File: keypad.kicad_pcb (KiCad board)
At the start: 2 copper layers, 3.6 x 3.2 mm, 14 parts, among them J1 Capacitive touch buttons, SW1 SW_Push, SW2 SW_Push, SW3 SW_Push, U1 XIAO-ESP32-S3

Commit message: fixed pcb wiring sorry!!
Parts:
- removed the J1 at (69.0, 128.0)
- removed the J1 at (159.0, 109.0)
- removed the J1 at (124.0, 110.0)
- removed the J1 at (140.0, 128.0)
- removed the J1 at (176.0, 128.0)
- added ?: , , F.Cu at (110.0, 86.0)
- added ?: , , F.Cu at (124.0, 132.0)
- added ?: , , F.Cu at (141.0, 89.0)
- added ?: , , F.Cu at (157.0, 129.0)
- added ?: , , F.Cu at (61.0, 132.0)
- moved D3 58.4 mm to (64.0, 50.0)
- moved U1 55.9 mm to (90.0, 59.0), turned to 90 degrees
- moved D2 37.3 mm to (64.0, 58.0)
- moved SW1 36.0 mm to (114.0, 59.1)
- moved SW2 36.0 mm to (135.0, 59.1)
- moved SW3 36.0 mm to (156.0, 59.1)
- moved ? 18.7 mm to (93.0, 128.6)
- moved D1 18.5 mm to (64.0, 66.0)
- moved J1 12.9 mm to (76.0, 103.3)
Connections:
- U1 pad 10: /SWITCH3 -> /LED
- U1 pad 11: /LED -> /TOUCH7
- U1 pad 9: /TOUCH7 -> /SWITCH3
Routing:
- net /TOUCH7: track 0.00 -> 125.6 mm
- net GND: track 0.00 -> 121.3 mm, vias 0 -> 1
- net /TOUCH5: track 0.00 -> 90.6 mm
- net /TOUCH1: track 0.00 -> 85.2 mm
- net /TOUCH3: track 0.00 -> 64.3 mm
- net /SWITCH3: track 0.00 -> 60.6 mm
- net /TOUCH6: track 0.00 -> 55.1 mm
- net +3.3V: track 0.00 -> 43.8 mm, vias 0 -> 3
- net /LED: track 0.00 -> 38.3 mm
- net /SWITCH2: track 0.00 -> 37.1 mm
- net Net-(D1-DOUT): track 0.00 -> 32.1 mm, vias 0 -> 2
- net /TOUCH4: track 0.00 -> 27.9 mm
- net /TOUCH2: track 0.00 -> 25.1 mm
- net Net-(D2-DOUT): track 0.00 -> 23.2 mm, vias 0 -> 2
- net /SWITCH1: track 0.00 -> 12.9 mm

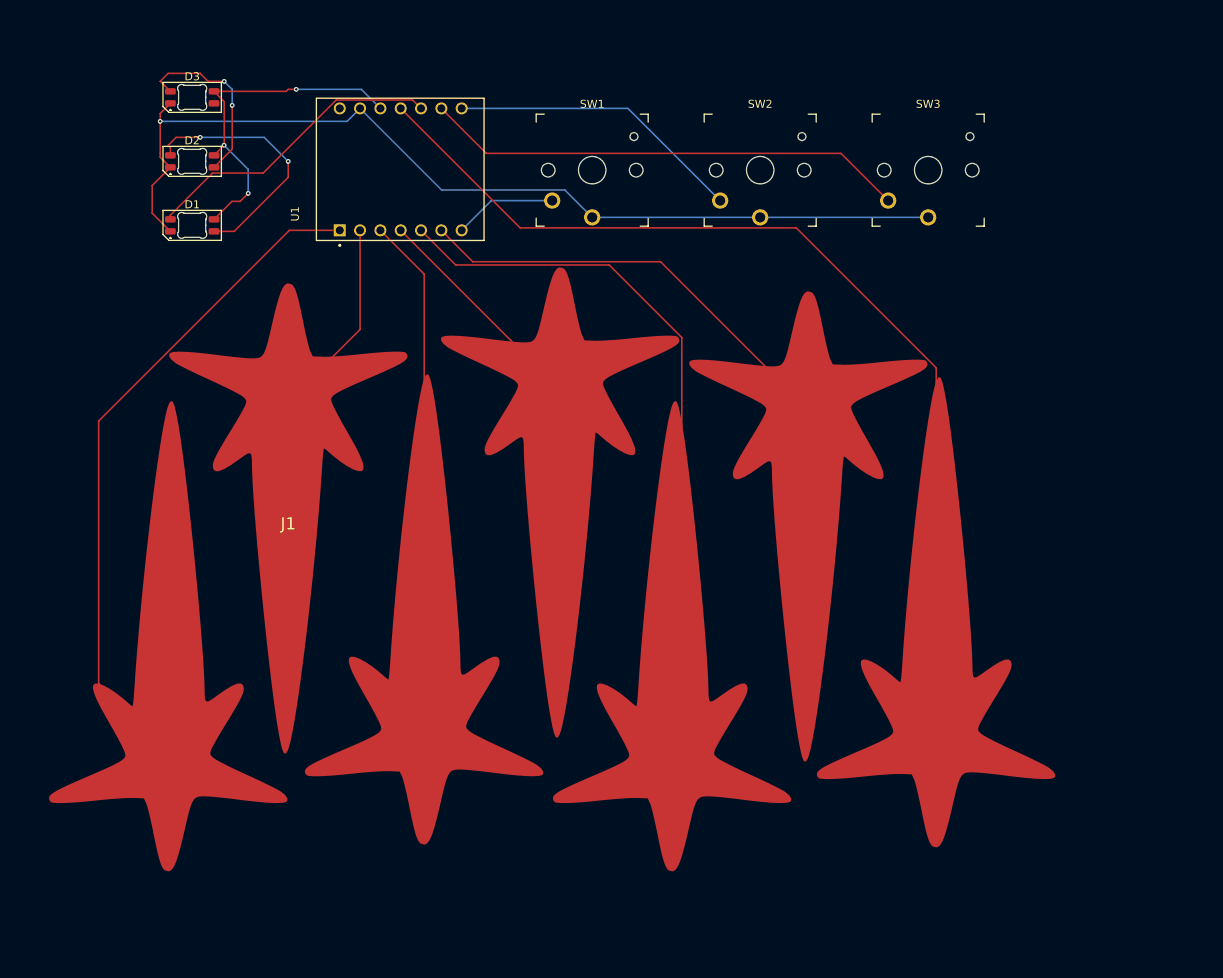
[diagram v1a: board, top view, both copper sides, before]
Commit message: fixed silkscreen
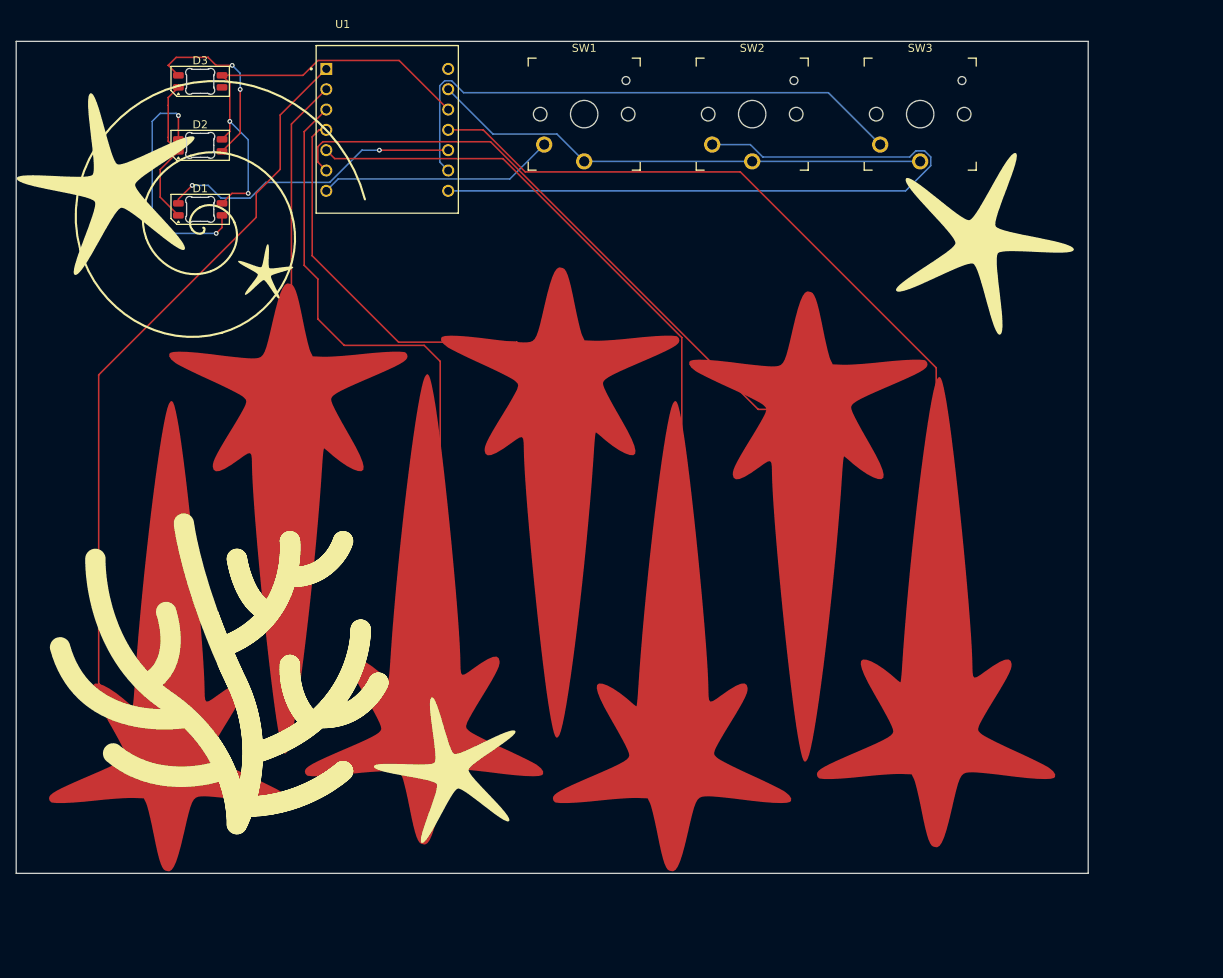
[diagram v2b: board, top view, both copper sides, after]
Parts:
- moved SW1 7.07 mm to (113.0, 52.1)
- moved SW2 7.07 mm to (134.0, 52.1)
- moved SW3 7.07 mm to (155.0, 52.1)
- moved U1 5.26 mm to (88.4, 54.0), turned to 0 degrees
- moved D1 2.24 mm to (65.0, 64.0)
- moved D2 2.24 mm to (65.0, 56.0)
- moved D3 2.24 mm to (65.0, 48.0)
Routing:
- net /SWITCH2: track 37.1 -> 91.3 mm
- net GND: track 121.3 -> 81.7 mm, vias 1 -> 0
- net /TOUCH3: track 64.3 -> 92.0 mm
- net /TOUCH4: track 27.9 -> 54.7 mm
- net /TOUCH6: track 55.1 -> 78.8 mm
- net /SWITCH1: track 12.9 -> 29.6 mm
- net /TOUCH5: track 90.6 -> 106.6 mm
- net /TOUCH2: track 25.1 -> 41.0 mm
- net /TOUCH1: track 85.2 -> 100.9 mm
- net +3.3V: track 43.8 -> 54.1 mm, vias 3 -> 2
- net /SWITCH3: track 60.6 -> 69.6 mm
- net /TOUCH7: track 125.6 -> 118.5 mm
- net Net-(D1-DOUT): track 32.1 -> 30.7 mm
- net /LED: track 38.3 -> 38.1 mm, vias 0 -> 2
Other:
- board size 3.6 x 3.2 mm -> 134 x 104 mm
